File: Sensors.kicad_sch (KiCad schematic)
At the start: 13 parts, among them U15 TPRT9013-33, U16 ICM-42688-P, U17 BMP280, U18 INA230

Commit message: Net nodes
Added the missing net nodes in the schematic.
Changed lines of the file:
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@@
 		(on_board yes)
 		(dnp no)
-		(fields_autoplaced yes)
 		(property "Reference" "C81"
-			(at 88.9 71.1199 0)
+			(at 77.724 71.12 0)
 			(effects
 				(font
@@
 		)
 		(property "Value" "10u"
-			(at 88.9 73.6599 0)
+			(at 77.724 73.66 0)
 			(effects
 				(font

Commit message: Board outline and net nodes
Added an initial board outline.
Updated net nodes definitions.
Updated board rules for manufacturing.
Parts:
- U18: footprint Package_DFN_QFN:VQFN-16-1EP_3x3mm_P0.5mm_EP1.6x1.6mm_ThermalVias -> Custom_Parts:VQFN-16-1EP_3x3mm_P0.5mm_EP1.6x1.6mm_ThermalVias
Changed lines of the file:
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@@
 			)
 		)
-		(property "Footprint" "Package_DFN_QFN:VQFN-16-1EP_3x3mm_P0.5mm_EP1.6x1.6mm_ThermalVias"
+		(property "Footprint" "Custom_Parts:VQFN-16-1EP_3x3mm_P0.5mm_EP1.6x1.6mm_ThermalVias"
 			(at 220.98 134.62 0)
 			(effects

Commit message: ESC layout and footprints
Added the initial ESC layout.
Updated some footprints for compatibility.
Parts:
- renumbered C79 to C83, C80 to C84, C81 to C85, C82 to C86, C83 to C87, C84 to C88, C85 to C89
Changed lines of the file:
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@@
 		(dnp no)
 		(fields_autoplaced yes)
-		(property "Reference" "C79"
+		(property "Reference" "C83"
 			(at 64.77 100.3299 0)
 			(effects
@@
 			(project "ThunderHorse"
 				(path "/ac187c6c-fa53-41cc-bce1-6f39a42a92e8/593939c9-ca21-46a5-baaf-5c6ecc4a9199"
-					(reference "C79")
+					(reference "C83")
 					(unit 1)
 				)
@@
 		(on_board yes)
 		(dnp no)
-		(property "Reference" "C85"
+		(property "Reference" "C89"
 			(at 227.33 110.49 0)
 			(effects
@@
 			(project "ThunderHorse"
 				(path "/ac187c6c-fa53-41cc-bce1-6f39a42a92e8/593939c9-ca21-46a5-baaf-5c6ecc4a9199"
-					(reference "C85")
+					(reference "C89")
 					(unit 1)
 				)
@@
 		(dnp no)
 		(fields_autoplaced yes)
-		(property "Reference" "C83"
+		(property "Reference" "C87"
 			(at 214.63 57.1499 0)
 			(effects
@@
 			(project "ThunderHorse"
 				(path "/ac187c6c-fa53-41cc-bce1-6f39a42a92e8/593939c9-ca21-46a5-baaf-5c6ecc4a9199"
-					(reference "C83")
+					(reference "C87")
 					(unit 1)
 				)
@@
 		(dnp no)
 		(fields_autoplaced yes)
-		(property "Reference" "C80"
+		(property "Reference" "C84"
 			(at 76.2 100.3299 0)
 			(effects
@@
 			(project "ThunderHorse"
 				(path "/ac187c6c-fa53-41cc-bce1-6f39a42a92e8/593939c9-ca21-46a5-baaf-5c6ecc4a9199"
-					(reference "C80")
+					(reference "C84")
 					(unit 1)
 				)
@@
 		(on_board yes)
 		(dnp no)
-		(property "Reference" "C81"
+		(property "Reference" "C85"
 			(at 77.724 71.12 0)
 			(effects
@@
 			(project "ThunderHorse"
 				(path "/ac187c6c-fa53-41cc-bce1-6f39a42a92e8/593939c9-ca21-46a5-baaf-5c6ecc4a9199"
-					(reference "C81")
+					(reference "C85")
 					(unit 1)
 				)
@@
 		(dnp no)
 		(fields_autoplaced yes)
-		(property "Reference" "C82"
+		(property "Reference" "C86"
 			(at 114.3 71.1199 0)
 			(effects
@@
 			(project "ThunderHorse"
 				(path "/ac187c6c-fa53-41cc-bce1-6f39a42a92e8/593939c9-ca21-46a5-baaf-5c6ecc4a9199"
-					(reference "C82")
+					(reference "C86")
 					(unit 1)
 				)
@@
 		(dnp no)
 		(fields_autoplaced yes)
-		(property "Reference" "C84"
+		(property "Reference" "C88"
 			(at 226.06 57.1499 0)
 			(effects
@@
 			(project "ThunderHorse"
 				(path "/ac187c6c-fa53-41cc-bce1-6f39a42a92e8/593939c9-ca21-46a5-baaf-5c6ecc4a9199"
-					(reference "C84")
-					(unit 1)
-				)
+					(reference "C88")
+					(unit 1)
+				)

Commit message: Initial layout
Completed an initial layout of the main components.

TODO
Route the ESCs and check the result.
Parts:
- C90: renamed from C89; footprint Capacitor_SMD:C_0201_0603Metric -> Capacitor_SMD:C_0603_1608Metric
- renumbered C83 to C84, C84 to C85, C85 to C86, C86 to C87, C87 to C88, C88 to C89, U15 to U16, U16 to U17, U17 to U18, U18 to U19
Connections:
- net 3V3: now also U18.2 (CSB), U18.5 (SDO)
- net 3V3_IMU: no longer U18.2 (CSB), U18.5 (SDO)

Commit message: ESC layout
Updated the layout for the final ESC.
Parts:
- C88, C89: footprint Capacitor_SMD:C_0201_0603Metric -> Capacitor_SMD:C_0603_1608Metric
- U18: footprint Package_LGA:Bosch_LGA-8_2x2.5mm_P0.65mm_ClockwisePinNumbering -> Custom_Parts:LGA-8_2x2.5mm_P0.65mm
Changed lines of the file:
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@@
 			)
 		)
-		(property "Footprint" "Package_LGA:Bosch_LGA-8_2x2.5mm_P0.65mm_ClockwisePinNumbering"
+		(property "Footprint" "Custom_Parts:LGA-8_2x2.5mm_P0.65mm"
 			(at 198.12 82.55 0)
 			(effects
@@
 			)
 		)
-		(property "Footprint" "Capacitor_SMD:C_0201_0603Metric"
+		(property "Footprint" "Capacitor_SMD:C_0603_1608Metric"
 			(at 211.7852 62.23 0)
 			(effects
@@
 			)
 		)
-		(property "Footprint" "Capacitor_SMD:C_0201_0603Metric"
+		(property "Footprint" "Capacitor_SMD:C_0603_1608Metric"
 			(at 223.2152 62.23 0)
 			(effects

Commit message: MCU layout
Started the MCU layout.

TODO:
Check the previous iterations.
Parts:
- added R91, R92: 5.1K, Resistor_SMD:R_0603_1608Metric, symbol Device:R
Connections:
- net 3V3: now also R91.1, R92.1
- net SENS_SCL: now also R91.2
- net SENS_SDA: now also R92.2
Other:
- moved on the sheet: C88, C89, U18

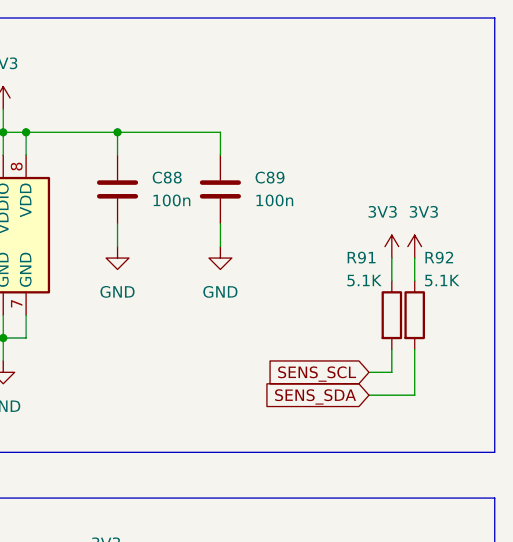
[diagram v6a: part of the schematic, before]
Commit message: MCU layout
Updated the schematic labels.
Continued the MCU layout.
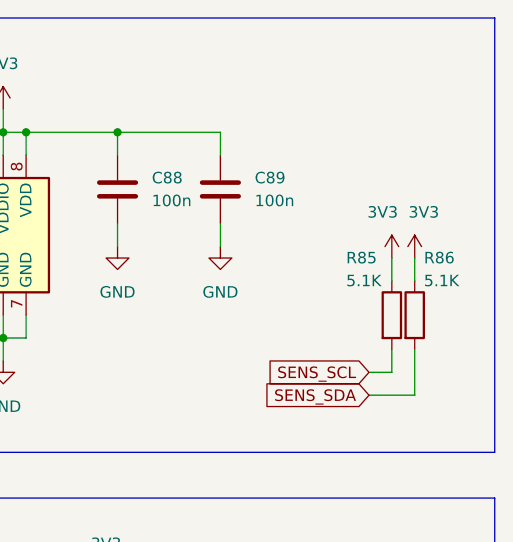
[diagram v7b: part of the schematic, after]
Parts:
- renumbered R91 to R85, R92 to R86
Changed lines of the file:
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@@
 		(dnp no)
 		(fields_autoplaced yes)
-		(property "Reference" "#PWR0160"
+		(property "Reference" "#PWR0161"
 			(at 168.91 132.08 0)
 			(effects
@@
 			(project "ThunderHorse"
 				(path "/ac187c6c-fa53-41cc-bce1-6f39a42a92e8/593939c9-ca21-46a5-baaf-5c6ecc4a9199"
-					(reference "#PWR0160")
+					(reference "#PWR0161")
 					(unit 1)
 				)
@@
 		(dnp no)
 		(fields_autoplaced yes)
-		(property "Reference" "#PWR0172"
+		(property "Reference" "#PWR0174"
 			(at 234.95 124.46 0)
 			(effects
@@
 			(project ""
 				(path "/ac187c6c-fa53-41cc-bce1-6f39a42a92e8/593939c9-ca21-46a5-baaf-5c6ecc4a9199"
-					(reference "#PWR0172")
+					(reference "#PWR0174")
 					(unit 1)
 				)
@@
 		(on_board yes)
 		(dnp no)
-		(property "Reference" "R91"
+		(property "Reference" "R85"
 			(at 227.33 66.04 0)
 			(effects
@@
 			(project "ThunderHorse"
 				(path "/ac187c6c-fa53-41cc-bce1-6f39a42a92e8/593939c9-ca21-46a5-baaf-5c6ecc4a9199"
-					(reference "R91")
+					(reference "R85")
 					(unit 1)
 				)
@@
 		(on_board yes)
 		(dnp no)
-		(property "Reference" "R92"
+		(property "Reference" "R86"
 			(at 235.966 66.04 0)
 			(effects
@@
 			(project "ThunderHorse"
 				(path "/ac187c6c-fa53-41cc-bce1-6f39a42a92e8/593939c9-ca21-46a5-baaf-5c6ecc4a9199"
-					(reference "R92")
+					(reference "R86")
 					(unit 1)
 				)
@@
 		(on_board yes)
 		(dnp no)
-		(property "Reference" "#PWR0212"
+		(property "Reference" "#PWR0172"
 			(at 232.41 69.85 0)
 			(effects
@@
 			(project "ThunderHorse"
 				(path "/ac187c6c-fa53-41cc-bce1-6f39a42a92e8/593939c9-ca21-46a5-baaf-5c6ecc4a9199"
-					(reference "#PWR0212")
+					(reference "#PWR0172")
 					(unit 1)
 				)
@@
 		(on_board yes)
 		(dnp no)
-		(property "Reference" "#PWR0213"
+		(property "Reference" "#PWR0173"
 			(at 234.95 69.85 0)
 			(effects
@@
 			(project "ThunderHorse"
 				(path "/ac187c6c-fa53-41cc-bce1-6f39a42a92e8/593939c9-ca21-46a5-baaf-5c6ecc4a9199"
-					(reference "#PWR0213")
+					(reference "#PWR0173")
 					(unit 1)
 				)
@@
 		(on_board yes)
 		(dnp no)
-		(property "Reference" "#PWR0161"
+		(property "Reference" "#PWR0160"
 			(at 161.29 66.04 0)
 			(effects
@@
 			(project "ThunderHorse"
 				(path "/ac187c6c-fa53-41cc-bce1-6f39a42a92e8/593939c9-ca21-46a5-baaf-5c6ecc4a9199"
-					(reference "#PWR0161")
-					(unit 1)
-				)
+					(reference "#PWR0160")
+					(unit 1)
+				)

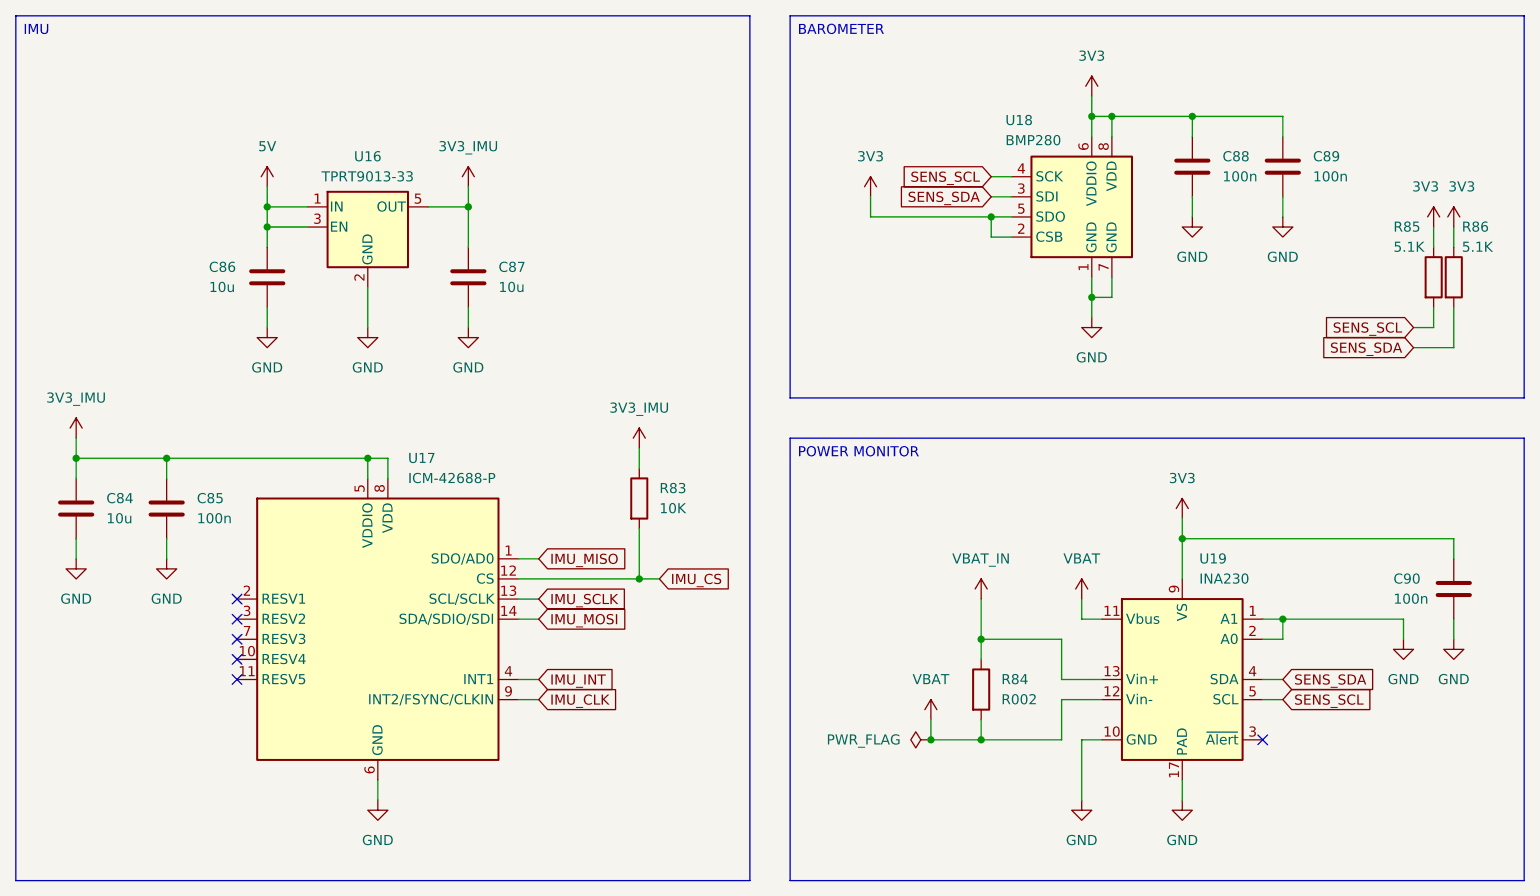
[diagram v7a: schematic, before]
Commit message: Schematic revision
Added an ESP32 C3 for the ELRS receiver.
Updated the protection approach for the board.
Updated the net nodes.
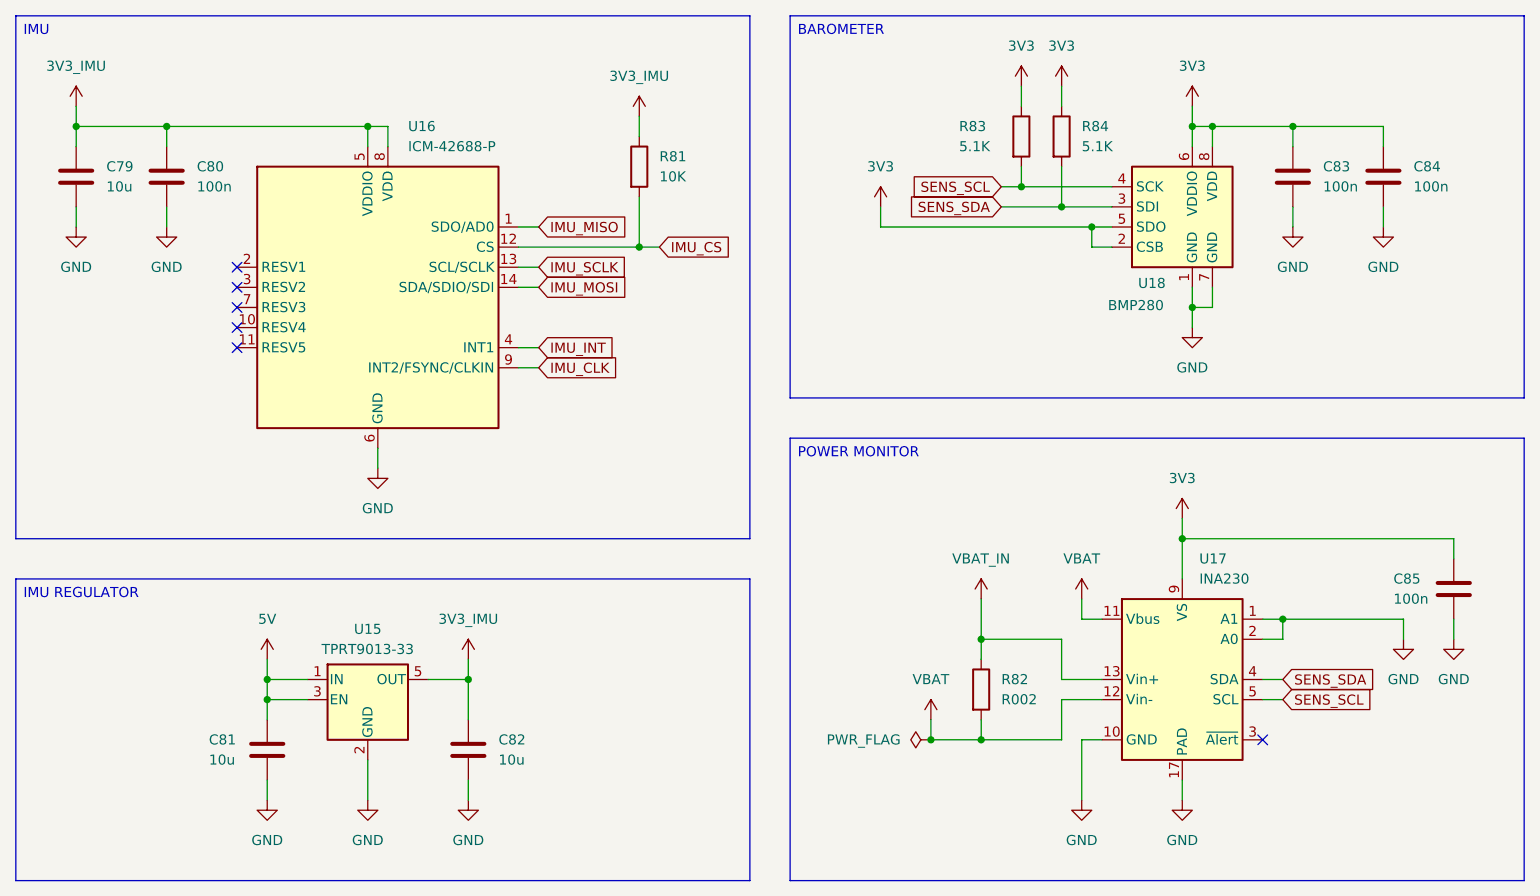
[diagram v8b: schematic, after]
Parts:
- removed R85, R86: 5.1K, Resistor_SMD:R_0603_1608Metric, symbol Device:R
- added R83, R84: 5.1K, Resistor_SMD:R_0603_1608Metric, symbol Device:R
- renumbered C84 to C79, C85 to C80, C86 to C81, C87 to C82, C88 to C83, C89 to C84, C90 to C85, R83 to R81, R84 to R82, U16 to U15, U17 to U16, U19 to U17
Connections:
- net 3V3: now also R83.1, R84.1
- net SENS_SCL: now also R83.2
- net SENS_SDA: now also R84.2
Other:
- moved on the sheet: C79, C80, C81, C82, C83, C84, R81, U15, U16, U18
